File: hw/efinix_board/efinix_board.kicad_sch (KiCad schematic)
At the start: 0 parts

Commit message: Start working on sdram
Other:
- added sheet sdram (sdram.kicad_sch)
- sheet fpga ports: added A[0..12], BA[0..1], CLK, DQ[0..15], LQDM, UQDM, ~{CAS}, ~{CKE}, ~{CS}, ~{RAS}, ~{WE}; removed none

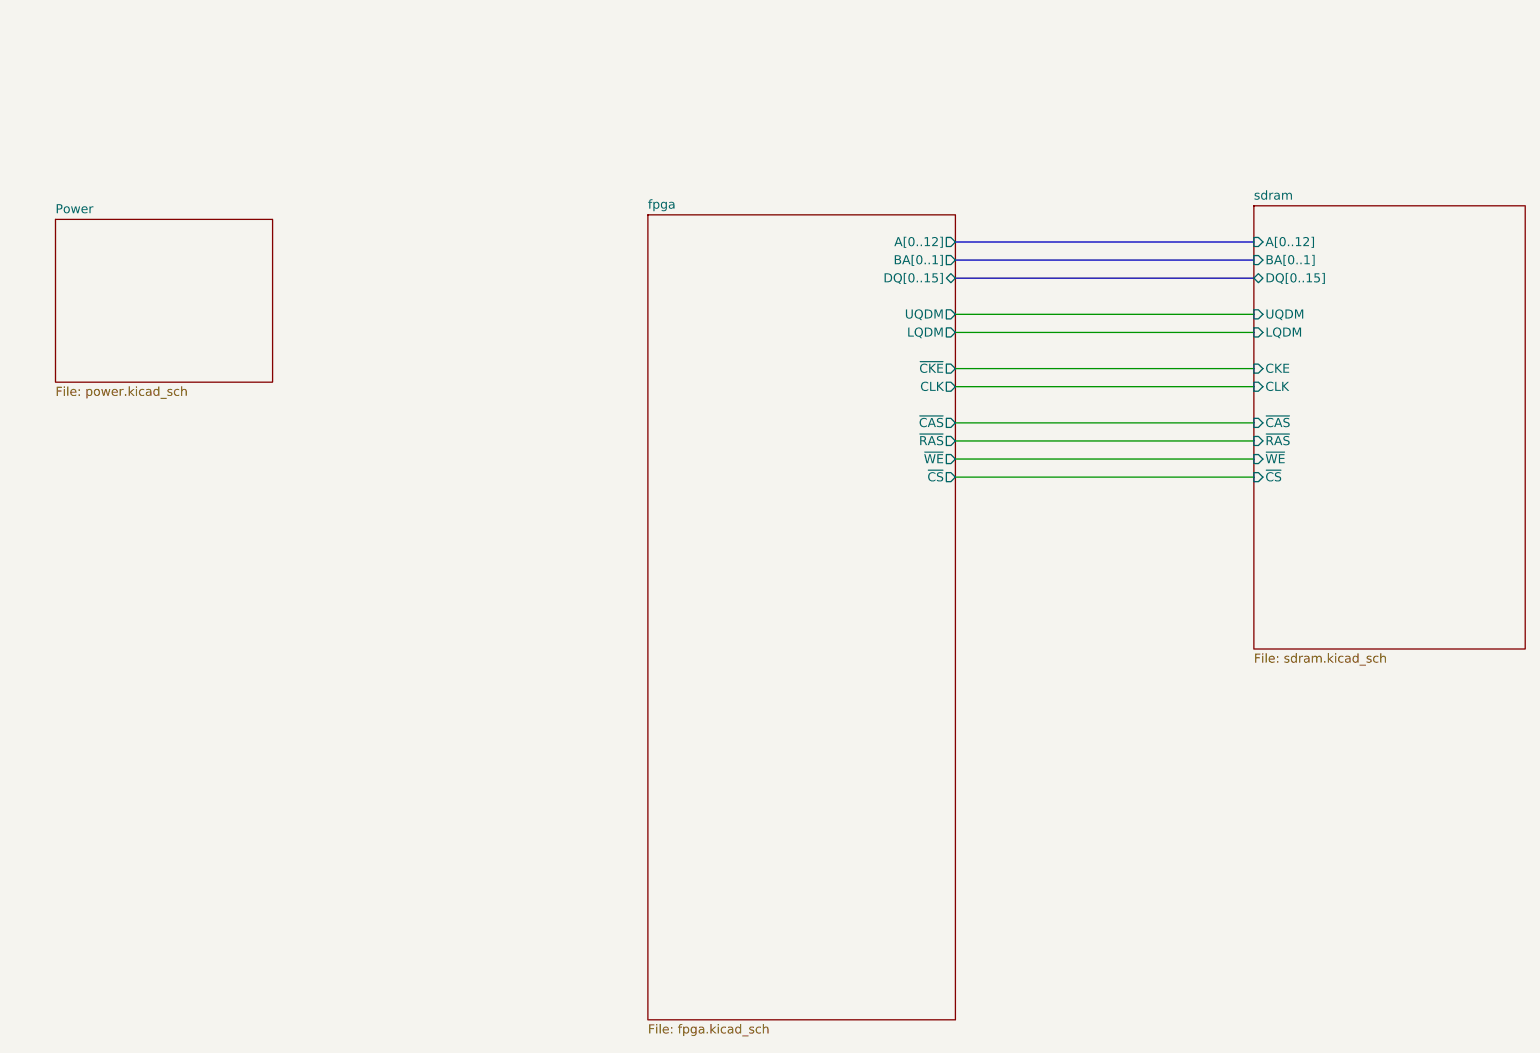
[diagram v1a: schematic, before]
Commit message: Add CPU and begin sch/layout
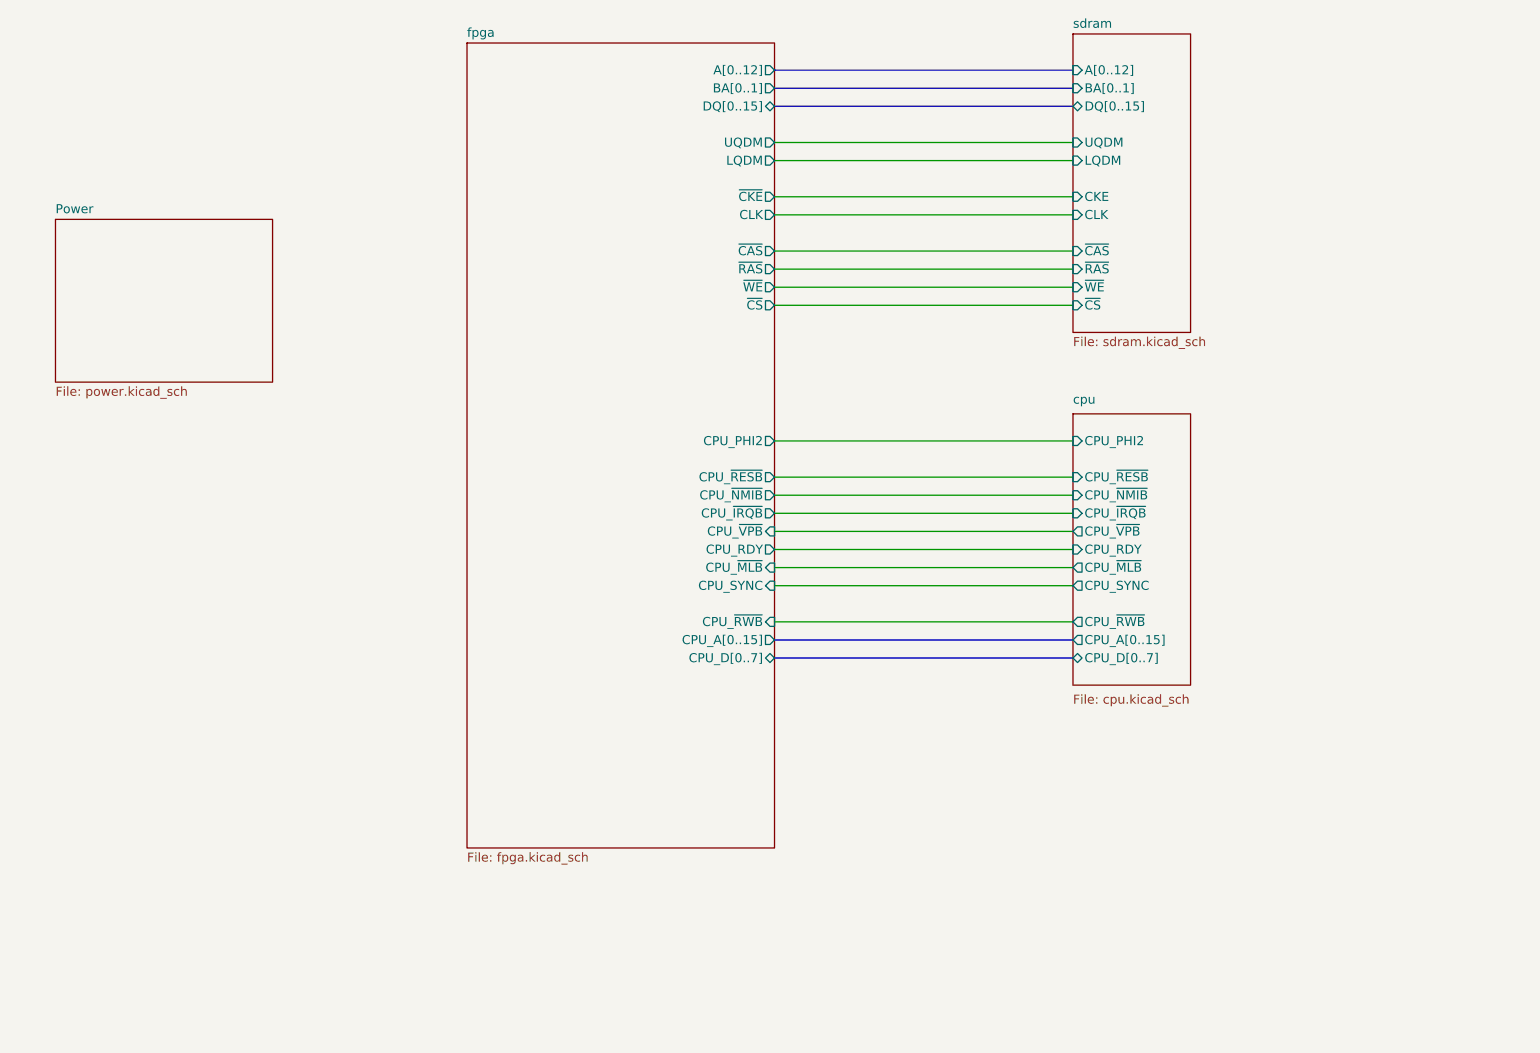
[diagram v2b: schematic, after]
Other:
- added sheet cpu (cpu.kicad_sch)
- sheet fpga ports: added CPU_A[0..15], CPU_D[0..7], CPU_PHI2, CPU_RDY, CPU_SYNC, CPU_~{IRQB}, CPU_~{MLB}, CPU_~{NMIB}, CPU_~{RESB}, CPU_~{RWB}, CPU_~{VPB}; removed none

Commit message: Update schematics and board
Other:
- added sheet Config (config.kicad_sch)
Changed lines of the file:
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@@
+    )
+  )
+  (sheet (at 36.83 83.82) (size 35.56 22.86) (fields_autoplaced)
+    (stroke (width 0.1524) (type solid) (color 0 0 0 0))
+    (fill (color 0 0 0 0.0000))
+    (property "Sheet name" "Config" (id 0) (at 36.83 83.1084 0)
+      (effects (font (size 1.27 1.27)) (justify left bottom))
+    )
+    (property "Sheet file" "config.kicad_sch" (id 1) (at 36.83 107.2646 0)
+      (effects (font (size 1.27 1.27)) (justify left top))
     )
   )
@@
     (path "/c77fe4eb-8f23-4f78-be9b-3f61160b1ef8" (page "4"))
     (path "/e900ed5d-98f6-483b-b296-7f8a7c9df9c0" (page "5"))
+    (path "/8371e888-d4b4-45f1-a119-675cfa8bd3fc" (page "6"))
   )
   (symbol_instances
@@
       (reference "#PWR024") (unit 1) (value "GND") (footprint "")
     )
+    (path "/5274a8df-1402-4d22-933d-856f39add0b6/d33a3e2f-ef74-4fec-bba4-b77eee1a6b47"
+      (reference "#PWR025") (unit 1) (value "+3V3") (footprint "")
+    )
+    (path "/5274a8df-1402-4d22-933d-856f39add0b6/fb24ddba-ae01-47d9-98b7-fca8e90e451a"
+      (reference "#PWR026") (unit 1) (value "GND") (footprint "")
+    )
+    (path "/5274a8df-1402-4d22-933d-856f39add0b6/ed5019b6-29fe-4512-8c2b-9b7ee87e3700"
+      (reference "#PWR027") (unit 1) (value "+3V3") (footprint "")
+    )
+    (path "/5274a8df-1402-4d22-933d-856f39add0b6/9882d69f-4f70-4952-b095-aba5e6f42239"
+      (reference "#PWR028") (unit 1) (value "GND") (footprint "")
+    )
+    (path "/5274a8df-1402-4d22-933d-856f39add0b6/11d503e3-ca6c-482b-a96b-1610f6db0399"
+      (reference "#PWR029") (unit 1) (value "+3V3") (footprint "")
+    )
     (path "/9320c3d1-2023-45d4-8e90-9efc5295795d/aa03a76f-06ea-43db-9386-c40916de89ee"
       (reference "#PWR0101") (unit 1) (value "+3V3") (footprint "")
@@
       (reference "R7") (unit 1) (value "100k") (footprint "Resistor_SMD:R_0402_1005Metric")
     )
+    (path "/5274a8df-1402-4d22-933d-856f39add0b6/0cb6c0ca-dc5a-487f-bd77-63598cee5bd8"
+      (reference "R8") (unit 1) (value "100k") (footprint "Resistor_SMD:R_0402_1005Metric")
+    )
+    (path "/5274a8df-1402-4d22-933d-856f39add0b6/b2357538-2a0d-4122-8864-407cfb02c6a5"
+      (reference "R9") (unit 1) (value "33R") (footprint "Resistor_SMD:R_0402_1005Metric")
+    )
+    (path "/5274a8df-1402-4d22-933d-856f39add0b6/7bc3fe74-088e-46c9-9527-ed2fb2858bd2"
+      (reference "R10") (unit 1) (value "100k") (footprint "Resistor_SMD:R_0402_1005Metric")
+    )
     (path "/e900ed5d-98f6-483b-b296-7f8a7c9df9c0/17a5239f-df2c-4a55-b844-54dd7afaf74d"
       (reference "R501") (unit 1) (value "10k") (footprint "Resistor_SMD:R_0402_1005Metric")
@@
       (reference "R507") (unit 1) (value "10k") (footprint "Resistor_SMD:R_0402_1005Metric")
     )
+    (path "/5274a8df-1402-4d22-933d-856f39add0b6/1645b139-70c0-4e26-925f-1dd1e52908aa"
+      (reference "SW1") (unit 1) (value "SW_Push") (footprint "Button_Switch_THT:SW_1825966-1")
+    )
     (path "/5274a8df-1402-4d22-933d-856f39add0b6/7247d2ec-daab-41c5-8cf3-01f60e9cd959"
       (reference "U1") (unit 1) (value "T20F256") (footprint "Package_BGA:BGA-256_14.0x14.0mm_Layout16x16_P0.8mm_Ball0.45mm_Pad0.32mm_NSMD")
     )
-    (path "/9320c3d1-2023-45d4-8e90-9efc5295795d/a9311994-aa47-45be-aab6-e6cde03c0d67"
+    (path "/8371e888-d4b4-45f1-a119-675cfa8bd3fc/89a4c0c0-2869-46c6-855d-870c75650034"
       (reference "U1") (unit 2) (value "T20F256") (footprint "Package_BGA:BGA-256_14.0x14.0mm_Layout16x16_P0.8mm_Ball0.45mm_Pad0.32mm_NSMD")
     )
@@
       (reference "U4") (unit 2) (value "NDS36PT5") (footprint "Package_SO:TSOP-II-54_22.2x10.16mm_P0.8mm")
     )
+    (path "/5274a8df-1402-4d22-933d-856f39add0b6/b49107d0-43e4-49e5-bfa0-8b9e5b174d94"
+      (reference "U5") (unit 1) (value "ADM6713") (footprint "Package_SC:ADM6711TAKSZ-REEL7")
+    )
+    (path "/8371e888-d4b4-45f1-a119-675cfa8bd3fc/eb039c2b-641b-45e3-8635-21ac9e8cedf6"
+      (reference "U6") (unit 1) (value "FT2232HL") (footprint "Package_QFP:LQFP-64_10x10mm_P0.5mm")
+    )
     (path "/e900ed5d-98f6-483b-b296-7f8a7c9df9c0/3e4a0029-cd42-4b46-98a4-aeb53f75a610"
